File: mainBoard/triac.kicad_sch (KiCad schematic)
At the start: 32 parts, among them J14 1714971, J18 1714971, Q1 IRLML6244TRPBF, Q2 IRLML6244TRPBF, U14 DS18B20+, U15 DS18B20+, U6 MOC3083S-TA1, U7 MOC3083S-TA1

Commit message: swapped MT pins on opto triacs
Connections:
- net L1_F2_OPTO_TOP: now also U6.6; no longer U6.4
- net L1_F3_OPTO_BOT: now also U7.6; no longer U7.4
- net L1_OPTO_BOT: now also U7.4; no longer U7.6
- net L1_OPTO_TOP: now also U6.4; no longer U6.6
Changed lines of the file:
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@@
 	)
 	(symbol
+		(lib_name "MOC3083M_1")
 		(lib_id "Relay_SolidState:MOC3083M")
 		(at 255.27 92.71 0)

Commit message: fine tuning
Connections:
- net L1_BOT: now also J14.1 (Pin_1); no longer J14.2 (Pin_2)
- net L1_F2_OPTO_TOP: now also U6.4; no longer U6.6
- net L1_OPTO_TOP: now also U6.6; no longer U6.4
- net L1_TOP: now also J18.1 (Pin_1); no longer J18.2 (Pin_2)
- net LN: now also J14.2 (Pin_2), J18.2 (Pin_2); no longer J14.1 (Pin_1), J18.1 (Pin_1)
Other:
- moved on the sheet: J14, J18
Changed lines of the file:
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@@
 	(symbol
 		(lib_id "Connector_Generic:Conn_01x02")
-		(at 143.51 152.4 90)
-		(unit 1)
-		(body_style 1)
-		(exclude_from_sim no)
-		(in_bom yes)
-		(on_board yes)
-		(in_pos_files yes)
-		(dnp no)
-		(fields_autoplaced yes)
+		(at 146.05 152.4 270)
+		(mirror x)
+		(unit 1)
+		(body_style 1)
+		(exclude_from_sim no)
+		(in_bom yes)
+		(on_board yes)
+		(in_pos_files yes)
+		(dnp no)
 		(property "Reference" "J14"
-			(at 148.59 151.13 90)
+			(at 140.97 151.13 90)
 			(show_name no)
 			(do_not_autoplace no)
@@
 		)
 		(property "Value" "1714971"
-			(at 148.59 153.67 90)
+			(at 140.97 153.67 90)
 			(show_name no)
 			(do_not_autoplace no)
@@
 		)
 		(property "Footprint" "PhoenixContact_MKDS_9mm:CONN_1714971_PXC"
-			(at 143.51 152.4 0)
-			(hide yes)
-			(show_name no)
-			(do_not_autoplace no)
-			(effects
-				(font
-					(size 1.27 1.27)
-				)
-			)
-		)
-		(property "Datasheet" ""
-			(at 143.51 152.4 0)
+			(at 146.05 152.4 0)
+			(hide yes)
+			(show_name no)
+			(do_not_autoplace no)
+			(effects
+				(font
+					(size 1.27 1.27)
+				)
+			)
+		)
+		(property "Datasheet" ""
+			(at 146.05 152.4 0)
 			(hide yes)
 			(show_name no)
@@
 		)
 		(property "Description" "Generic connector, single row, 01x02, script generated (kicad-library-utils/schlib/autogen/connector/)"
-			(at 143.51 152.4 0)
+			(at 146.05 152.4 0)
 			(hide yes)
 			(show_name no)
@@
 	(symbol
 		(lib_id "Connector_Generic:Conn_01x02")
-		(at 142.24 80.01 90)
-		(unit 1)
-		(body_style 1)
-		(exclude_from_sim no)
-		(in_bom yes)
-		(on_board yes)
-		(in_pos_files yes)
-		(dnp no)
-		(fields_autoplaced yes)
+		(at 144.78 80.01 270)
+		(mirror x)
+		(unit 1)
+		(body_style 1)
+		(exclude_from_sim no)
+		(in_bom yes)
+		(on_board yes)
+		(in_pos_files yes)
+		(dnp no)
 		(property "Reference" "J18"
-			(at 147.32 78.74 90)
+			(at 139.7 78.74 90)
 			(show_name no)
 			(do_not_autoplace no)
@@
 		)
 		(property "Value" "1714971"
-			(at 147.32 81.28 90)
+			(at 139.7 81.28 90)
 			(show_name no)
 			(do_not_autoplace no)
@@
 		)
 		(property "Footprint" "PhoenixContact_MKDS_9mm:CONN_1714971_PXC"
-			(at 142.24 80.01 0)
-			(hide yes)
-			(show_name no)
-			(do_not_autoplace no)
-			(effects
-				(font
-					(size 1.27 1.27)
-				)
-			)
-		)
-		(property "Datasheet" ""
-			(at 142.24 80.01 0)
+			(at 144.78 80.01 0)
+			(hide yes)
+			(show_name no)
+			(do_not_autoplace no)
+			(effects
+				(font
+					(size 1.27 1.27)
+				)
+			)
+		)
+		(property "Datasheet" ""
+			(at 144.78 80.01 0)
 			(hide yes)
 			(show_name no)
@@
 		)
 		(property "Description" "Generic connector, single row, 01x02, script generated (kicad-library-utils/schlib/autogen/connector/)"
-			(at 142.24 80.01 0)
-			(hide yes)
-			(show_name no)
+			(at 144.78 80.01 0)
+			(hide yes)
+			(show_name no)

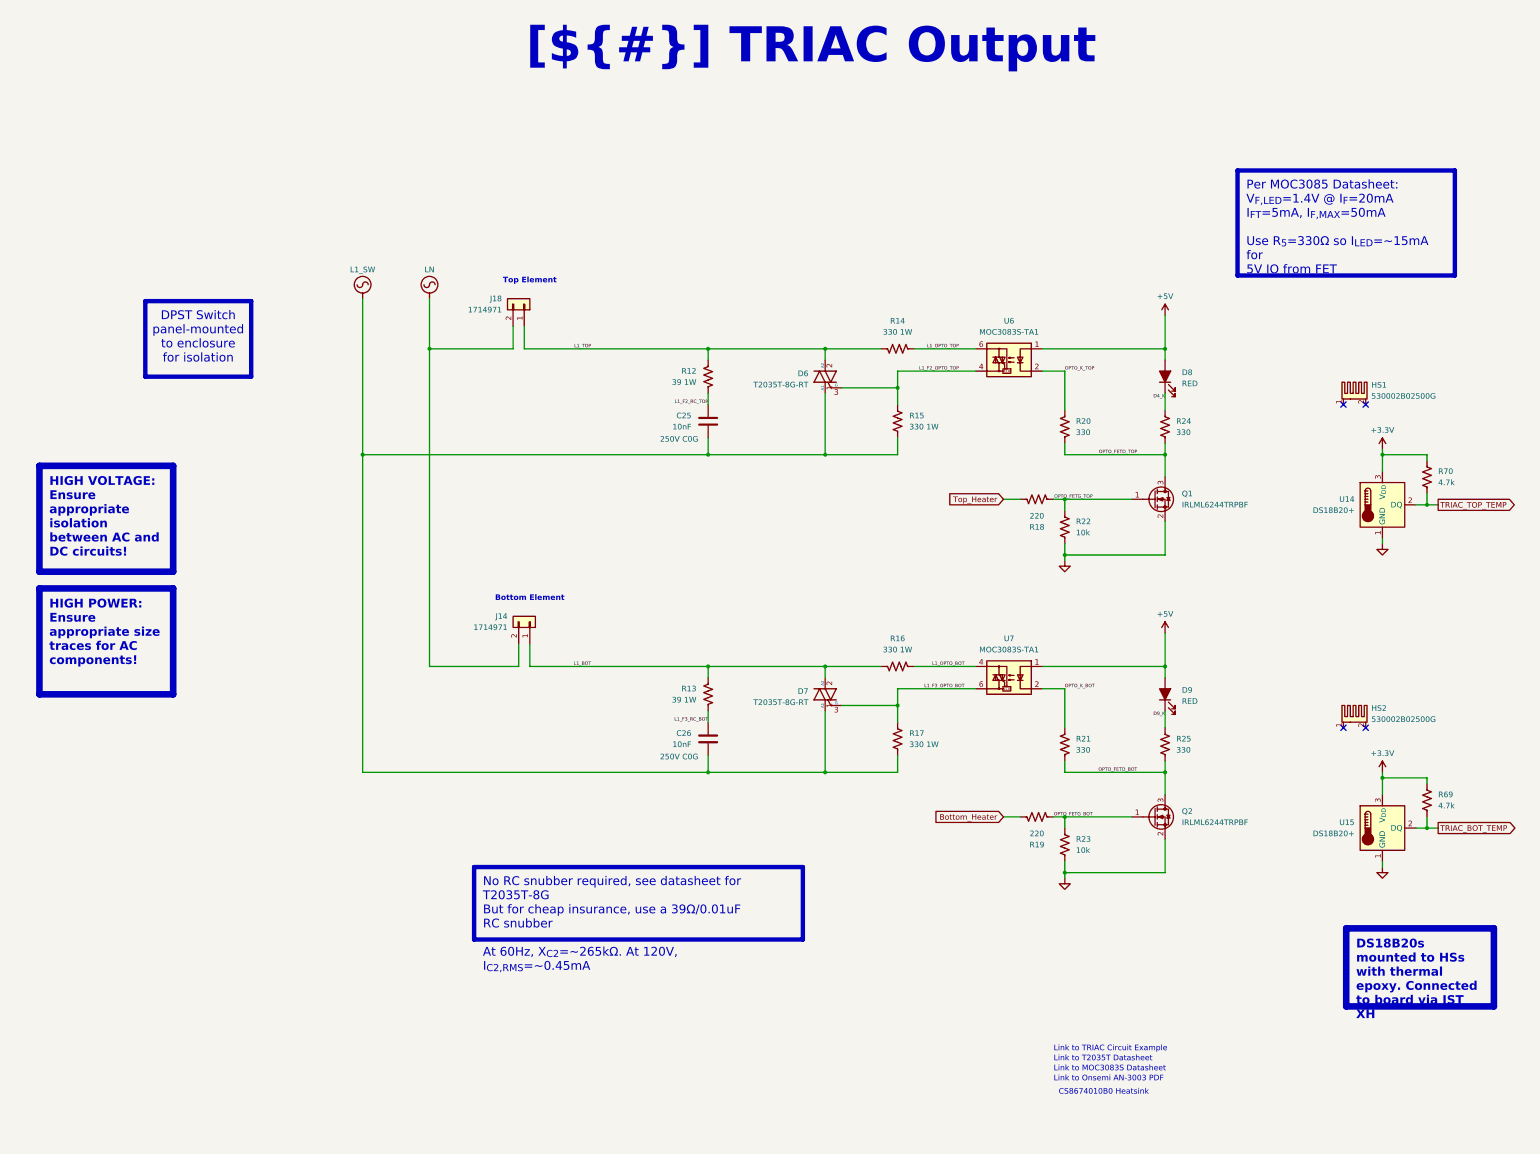
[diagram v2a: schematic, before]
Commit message: change to single 4" touchscreen for UI instead of keypad and buttons
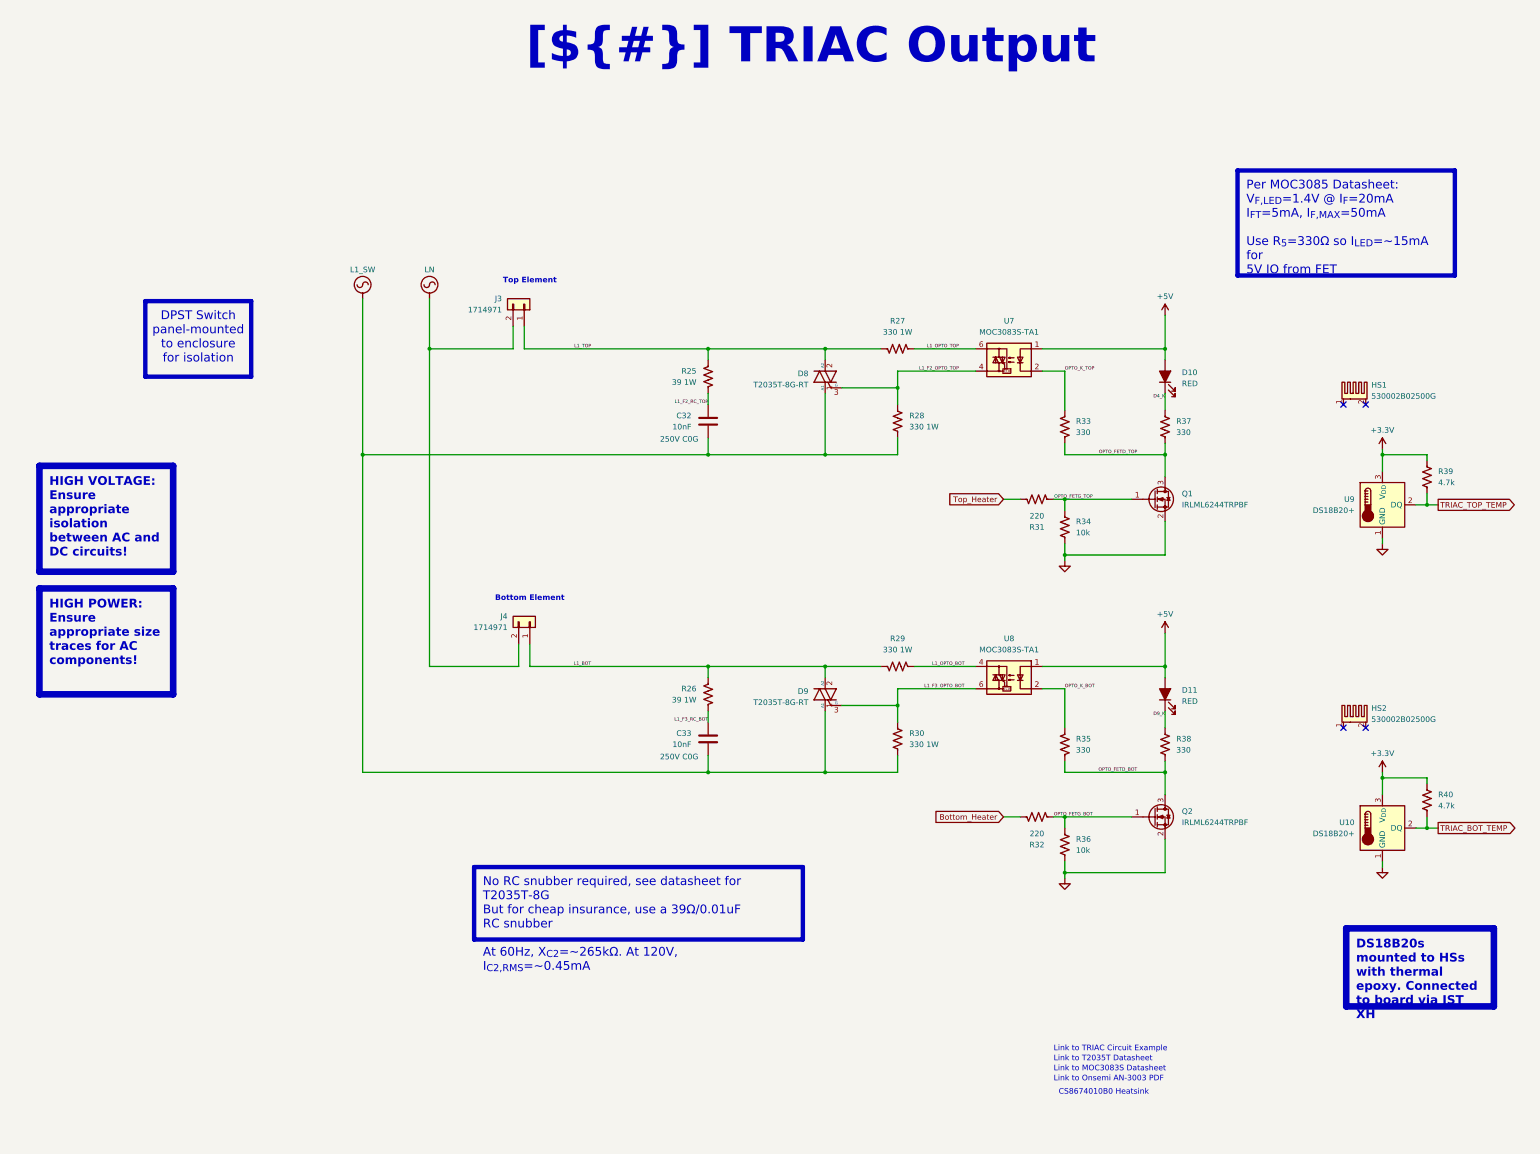
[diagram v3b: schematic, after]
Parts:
- renumbered C25 to C32, C26 to C33, D8 to D10, D9 to D11, D6 to D8, D7 to D9, J18 to J3, J14 to J4, R12 to R25, R13 to R26, R14 to R27, R15 to R28, R16 to R29, R17 to R30, R18 to R31, R19 to R32, R20 to R33, R22 to R34, R21 to R35, R23 to R36, R24 to R37, R25 to R38, R70 to R39, R69 to R40, U15 to U10, U6 to U7, U7 to U8, U14 to U9

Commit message: change to stm32f413 and add a QSPI SRAM
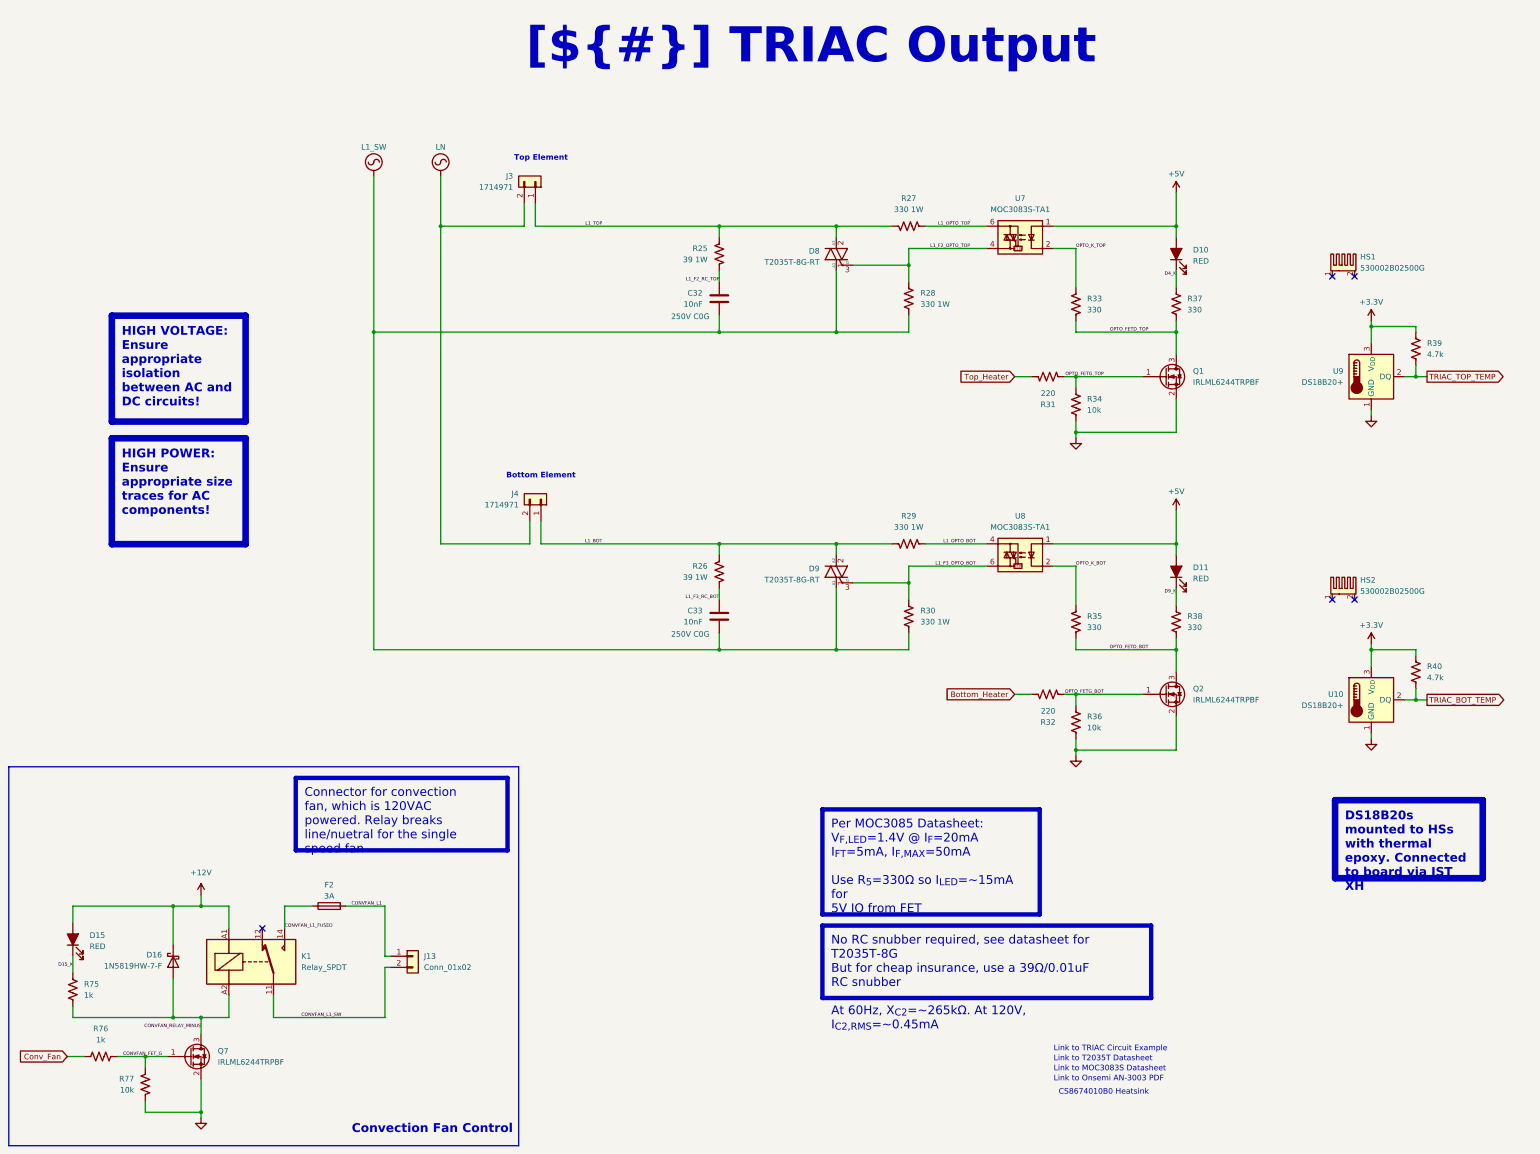
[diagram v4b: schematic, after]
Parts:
- added D15: RED, LED_SMD:LED_0603_1608Metric_Pad1.05x0.95mm_HandSolder, symbol Device:LED_Filled
- added D16: 1N5819HW-7-F, Diode_SMD:D_SOD-123, symbol Diode:1N5819
- added F2: 3A, Fuse:Fuseholder_Clip-5x20mm_Littelfuse_100_Inline_P20.50x4.60mm_D1.30mm_Horizontal, symbol Device:Fuse
- added J13: Conn_01x02, PhoenixContact_MKDS_9mm:CONN_1714971_PXC, symbol Connector_Generic:Conn_01x02
- added K1: Relay_SPDT, Relay_THT:Relay_SPDT_Finder_36.11, symbol Relay:Relay_SPDT
- added Q7: IRLML6244TRPBF, Package_TO_SOT_SMD:SOT-23, symbol Transistor_FET:IRLML6244
- added R75, R76: 1k, Resistor_SMD:R_0603_1608Metric_Pad0.98x0.95mm_HandSolder, symbol Device:R_US
- added R77: 10k, Resistor_SMD:R_0603_1608Metric_Pad0.98x0.95mm_HandSolder, symbol Device:R_US
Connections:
- net GND: now also Q7.2 (S), R77.2
- new net +12V: D15.2 (A), D16.1 (K), K1.A1
- new net CONVFAN_FET_G: Q7.1 (G), R76.2, R77.1
- new net CONVFAN_L1: F2.2, J13.1 (Pin_1)
- new net CONVFAN_L1_FUSED: F2.1, K1.14
- new net CONVFAN_L1_SW: J13.2 (Pin_2), K1.11
- new net CONVFAN_RELAY_MINUS: D16.2 (A), K1.A2, Q7.3 (D), R75.2
- new net Conv_Fan: R76.1
- new net D15_K: D15.1 (K), R75.1
- no-connect marks 4 -> 5
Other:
- note added: "Convection Fan Control"
- moved on the sheet: C32, C33, D10, D11, D8, D9, HS1, HS2, J3, J4, Q1, Q2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

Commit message: working on layout
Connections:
- net L1_F2_OPTO_TOP: now also U7.6; no longer U7.4
- net L1_OPTO_TOP: now also U7.4; no longer U7.6
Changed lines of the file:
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@@
 		(in_pos_files yes)
 		(dnp no)
-		(fields_autoplaced yes)
 		(property "Reference" "J13"
 			(at 121.92 228.5999 0)
